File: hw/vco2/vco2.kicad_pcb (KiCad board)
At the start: 4 copper layers, 30 x 128.5 mm, 85 parts, among them J1 Conn_02x08_Odd_Even, Q1 DNP, SW1 SW_SPDT, U1 SSI2131, U2 TL431BCDBZR, U4 TL072HxD, U5 TL072HxD

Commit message: Dual VCO board
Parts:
- removed G***: LOGO, elemental:elemental-4mm
- removed H2, H3, H4: MountingHole, MountingHole:MountingHole_3.5mm
- removed REF**: OSHW-Logo2_7.3x6mm_SilkScreen, Symbol:OSHW-Logo2_7.3x6mm_SilkScreen
- removed RV_CV2: 100k, Pot:RV9012NO
- removed SW1: SW_SPDT, Switch:SPDT big pads
- added C16: 100n, Capacitor_SMD:C_0805_2012Metric_Pad1.18x1.45mm_HandSolder, F.Cu at (56.5, 89.5)
- added C19: 100n, Capacitor_SMD:C_0603_1608Metric_Pad1.08x0.95mm_HandSolder, F.Cu at (153.0, 97.1)
- added C20: 100n, Capacitor_SMD:C_0603_1608Metric_Pad1.08x0.95mm_HandSolder, F.Cu at (153.0, 99.6)
- added C21: 100n, Capacitor_SMD:C_0805_2012Metric_Pad1.18x1.45mm_HandSolder, F.Cu at (179.1, 108.3)
- added C22: 100n, Capacitor_SMD:C_0603_1608Metric_Pad1.08x0.95mm_HandSolder, F.Cu at (153.0, 102.1)
- added C23: 100n, Capacitor_SMD:C_0603_1608Metric_Pad1.08x0.95mm_HandSolder, F.Cu at (153.0, 104.6)
- added C24: 100n X7R, Capacitor_SMD:C_0603_1608Metric_Pad1.08x0.95mm_HandSolder, F.Cu at (195.7, 81.6)
- added C25: 3.9n C0G, Capacitor_SMD:C_0603_1608Metric_Pad1.08x0.95mm_HandSolder, F.Cu at (195.7, 84.1)
- added C26: 10n, Capacitor_SMD:C_0603_1608Metric_Pad1.08x0.95mm_HandSolder, F.Cu at (195.7, 86.7)
- added C27: 100n X7R, Capacitor_SMD:C_0603_1608Metric_Pad1.08x0.95mm_HandSolder, F.Cu at (195.7, 89.2)
- added D3: LED wave out, LED_THT:LED_D3.0mm, F.Cu at (178.4, 98.6)
- added D4: LED wave out, LED_THT:LED_D3.0mm, F.Cu at (178.4, 104.0)
- added JP1: jumper, Jumper:SolderJumper-2_P1.3mm_Bridged2Bar_Pad1.0x1.5mm, F.Cu at (41.4, 85.3)
- added J_PULSE2: TS, Connector_Audio:Jack_3.5mm_QingPu_WQP-PJ398SM_Vertical_CircularHoles, F.Cu at (126.0, 138.2)
- added J_PWM2: TS, Connector_Audio:Jack_3.5mm_QingPu_WQP-PJ398SM_Vertical_CircularHoles, F.Cu at (132.0, 119.2)
- added J_SAW2: TS, Connector_Audio:Jack_3.5mm_QingPu_WQP-PJ398SM_Vertical_CircularHoles, F.Cu at (117.0, 136.2)
- added J_TRI2: TS, Connector_Audio:Jack_3.5mm_QingPu_WQP-PJ398SM_Vertical_CircularHoles, F.Cu at (135.0, 136.2)
- added R36: 32k, Resistor_SMD:R_0603_1608Metric_Pad0.98x0.95mm_HandSolder, F.Cu at (51.9, 93.9)
- added R37: 39k, Resistor_SMD:R_0603_1608Metric_Pad0.98x0.95mm_HandSolder, F.Cu at (51.9, 96.4)
- added R38: 49k9, Resistor_SMD:R_0603_1608Metric_Pad0.98x0.95mm_HandSolder, F.Cu at (51.9, 98.9)
- added R39: 10k, Resistor_SMD:R_0603_1608Metric_Pad0.98x0.95mm_HandSolder, F.Cu at (153.0, 107.1)
- added R40: 20k, Resistor_SMD:R_0603_1608Metric_Pad0.98x0.95mm_HandSolder, F.Cu at (153.0, 109.6)
- added R41: 1k, Resistor_SMD:R_0603_1608Metric_Pad0.98x0.95mm_HandSolder, F.Cu at (153.0, 112.1)
- added R42: 49k9, Resistor_SMD:R_0603_1608Metric_Pad0.98x0.95mm_HandSolder, F.Cu at (157.4, 97.1)
- added R43: 49k9, Resistor_SMD:R_0603_1608Metric_Pad0.98x0.95mm_HandSolder, F.Cu at (157.4, 99.6)
- added R44: 10k, Resistor_SMD:R_0603_1608Metric_Pad0.98x0.95mm_HandSolder, F.Cu at (157.4, 102.1)
- added R45: 250k, Resistor_SMD:R_0603_1608Metric_Pad0.98x0.95mm_HandSolder, F.Cu at (157.4, 104.6)
- added R46: 49k9, Resistor_SMD:R_0603_1608Metric_Pad0.98x0.95mm_HandSolder, F.Cu at (157.4, 107.1)
- added R49: 49k9, Resistor_SMD:R_0603_1608Metric_Pad0.98x0.95mm_HandSolder, F.Cu at (157.4, 109.6)
- added R50: 49k9, Resistor_SMD:R_0603_1608Metric_Pad0.98x0.95mm_HandSolder, F.Cu at (157.4, 112.1)
- added R51: 32k, Resistor_SMD:R_0603_1608Metric_Pad0.98x0.95mm_HandSolder, F.Cu at (161.7, 97.1)
- added R52: 10k, Resistor_SMD:R_0603_1608Metric_Pad0.98x0.95mm_HandSolder, F.Cu at (161.7, 99.6)
- added R53: 10k, Resistor_SMD:R_0603_1608Metric_Pad0.98x0.95mm_HandSolder, F.Cu at (161.7, 102.1)
- added R54: 10k, Resistor_SMD:R_0603_1608Metric_Pad0.98x0.95mm_HandSolder, F.Cu at (161.7, 104.6)
- added R55: 10k, Resistor_SMD:R_0603_1608Metric_Pad0.98x0.95mm_HandSolder, F.Cu at (161.7, 107.1)
- added R56: 39k, Resistor_SMD:R_0603_1608Metric_Pad0.98x0.95mm_HandSolder, F.Cu at (161.7, 109.6)
- added R57: 39k, Resistor_SMD:R_0603_1608Metric_Pad0.98x0.95mm_HandSolder, F.Cu at (161.7, 112.1)
- added R58: 39k, Resistor_SMD:R_0603_1608Metric_Pad0.98x0.95mm_HandSolder, F.Cu at (166.1, 97.1)
- added R59: 39k, Resistor_SMD:R_0603_1608Metric_Pad0.98x0.95mm_HandSolder, F.Cu at (166.1, 99.6)
- added R60: 1k, Resistor_SMD:R_0603_1608Metric_Pad0.98x0.95mm_HandSolder, F.Cu at (166.1, 102.1)
- added R61: 1k, Resistor_SMD:R_0603_1608Metric_Pad0.98x0.95mm_HandSolder, F.Cu at (166.1, 104.6)
- added R62: 1k, Resistor_SMD:R_0603_1608Metric_Pad0.98x0.95mm_HandSolder, F.Cu at (166.1, 107.1)
- added R63: 4k3, Resistor_SMD:R_0603_1608Metric_Pad0.98x0.95mm_HandSolder, F.Cu at (195.7, 91.7)
- added R64: 267k, Resistor_SMD:R_0603_1608Metric_Pad0.98x0.95mm_HandSolder, F.Cu at (195.7, 94.2)
- added R65: 499k, Resistor_SMD:R_0603_1608Metric_Pad0.98x0.95mm_HandSolder, F.Cu at (195.7, 96.7)
- added R66: 20k, Resistor_SMD:R_0603_1608Metric_Pad0.98x0.95mm_HandSolder, F.Cu at (195.7, 99.2)
- added R67: 270, Resistor_SMD:R_0603_1608Metric_Pad0.98x0.95mm_HandSolder, F.Cu at (195.7, 101.7)
- added RV_CALIB2: 10k 3266Y-103, Potentiometer_THT:Potentiometer_Bourns_3266Y_Vertical, F.Cu at (204.5, 94.9)
- added RV_PWM2: 20k, Pot:RV9012NO, F.Cu at (127.8, 65.0)
- added RV_RANGE2: 20k, Pot:RV9012NO, F.Cu at (121.4, 46.6)
- added RV_TUNE2: 20k, Pot:RV9012NO, F.Cu at (134.7, 46.6)
- added TP10: TestPoint_Alt, Holes:TP_0.9mm, F.Cu at (207.7, 96.4)
- added TP9: TestPoint_Alt, Holes:TP_0.9mm, F.Cu at (207.7, 93.4)
- added U3: TL072HxD, Package_SO:SOIC-8_3.9x4.9mm_P1.27mm, F.Cu at (43.5, 71.4)
- added U6: TL431BCDBV, Package_TO_SOT_SMD:SOT-23-5, F.Cu at (35.2, 83.5)
- added U7: TL072HxD, Package_SO:SOIC-8_3.9x4.9mm_P1.27mm, F.Cu at (172.5, 99.2)
- added U8: TL072HxD, Package_SO:SOIC-8_3.9x4.9mm_P1.27mm, F.Cu at (172.5, 105.8)
- added U9: SSI2131, Package_SO:STC_SOP-16_3.9x9.9mm_P1.27mm, F.Cu at (202.1, 86.3)
- C1, C13, C2, C3, C4, C5, C6, C8, J1, Q1, R10, R11, R12, R13, R20, R23, R24, R25, R32, R33, R34, R35, RV_CALIB1, U1: moved to F.Cu
- C7: value 2.2u -> 100n; footprint Capacitor_SMD:C_0805_2012Metric_Pad1.18x1.45mm_HandSolder -> Capacitor_SMD:C_0603_1608Metric_Pad1.08x0.95mm_HandSolder; moved to F.Cu
- D1: value LED sync -> LED wave out
- H1: footprint MountingHole:MountingHole_3.5mm -> MountingHole:MountingHole_3.2mm_M3_Pad
- J_CV1, J_CV2, J_FM1, J_PULSE1, J_PWM1, J_SAW1, J_SYNC1, J_TRI1: value AudioJack2_SwitchT -> TS
- R15: value 49k9 -> 10k; moved to F.Cu
- R16: value 1M -> 250k
- R17: value 49k9 -> 10k
- R18, R19: value 100k -> 49k9
- R27, R8: value 1k -> 39k; moved to F.Cu
- R28: value 0 -> 49k9; moved to F.Cu
- R29: value 0 -> 20k; moved to F.Cu
- R30: value 0 -> 1k; moved to F.Cu
- R31: value 0 -> 10k
- RV_PWM1, RV_RANGE1, RV_TUNE1: value 100k -> 20k
- U2: value TL431BCDBZR -> TL431BCDBZ; moved to F.Cu
- moved J1 109.7 mm to (25.9, 64.1), turned to 0 degrees
- moved TP7 88.5 mm to (178.2, 111.2)
- moved C13 84.7 mm to (34.8, 64.3), turned to 0 degrees
- moved R8 84.0 mm to (34.8, 66.8), turned to 0 degrees
- moved C1 81.8 mm to (34.8, 59.2), turned to 0 degrees
- moved J_CV1 80.2 mm to (90.0, 132.0)
- moved R25 79.7 mm to (39.2, 64.3), turned to 0 degrees
- moved R32 79.2 mm to (43.5, 59.2), turned to 0 degrees
- moved R33 78.7 mm to (43.5, 61.7), turned to 0 degrees
- moved C7 78.2 mm to (34.8, 61.7)
- moved R34 74.3 mm to (43.5, 64.3), turned to 0 degrees
- moved R35 72.5 mm to (43.5, 66.8), turned to 0 degrees
- moved J_CV2 71.2 mm to (121.0, 118.9), turned to 0 degrees
- moved TP3 66.5 mm to (45.7, 76.1)
- moved C2 65.8 mm to (34.8, 71.3), turned to 0 degrees
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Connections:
- net /BW_COMP renamed /Oscillator 1/BW_COMP
- net /LIN_FREQ renamed /LIN_FREQ1
- net /PULSE_OUT renamed /PULSE1
- net /SAW_OUT renamed /SAW1
- C1 pad 1: +2V5 -> +12V
- C10 pad 2: /HARD_SYNC -> /HARD_SYNC1
- C6 pad 1: /TCAP -> /Oscillator 1/TCAP
- C7 pad 1: /TCAP -> GND
- C7 pad 2: Net-(SW1-A) -> -12V
- D1 pad 2: /HARD_SYNC -> GND
- D2 pad 1: Net-(D2-K) -> GND
- D2 pad 2: Net-(D2-A) -> Net-(D1-K)
- J1 pad 14: unconnected-(J1-Pin_14-Pad14) -> Net-(J1-Pin_14)
- J_CV1 pad TN: GND -> BACKPLANE_CV
- J_CV2 pad TN: unconnected-(J_CV2-PadTN) -> Net-(J_CV1-PadT)
- J_PULSE1 pad T: Net-(J_PULSE1-PadT) -> Net-(C16-Pad2)
- Q1 pad 2: /HARD_SYNC -> ANTI_HANGUP
- R11 pad 1: /HF_TRACK -> /Oscillator 1/HF_TRACK
- R11 pad 2: /EXPO_FREQ -> /EXPO_FREQ1
- R12 pad 1: /HF_TRACK -> /Oscillator 1/HF_TRACK
- R14 pad 2: /EXPO_FREQ -> /EXPO_FREQ1
- R15 pad 1: Net-(R15-Pad1) -> Net-(U5B--)
- R15 pad 2: /EXPO_FREQ -> /TRI1
- R16 pad 2: /EXPO_FREQ -> /EXPO_FREQ1
- R17 pad 2: /EXPO_FREQ -> /EXPO_FREQ1
- R18 pad 2: /PWM_CTRL -> Net-(R18-Pad2)
- R19 pad 2: /PWM_CTRL -> Net-(R18-Pad2)
- R22 pad 1: /HARD_SYNC -> /HARD_SYNC1
- R25 pad 1: +2V5 -> Net-(U2-K)
- R26 pad 1: Net-(D2-K) -> Net-(R26-Pad1)
- R26 pad 2: GND -> Net-(D1-K)
- R27 pad 1: Net-(D1-K) -> Net-(U3B--)
- R27 pad 2: GND -> -2V5
- R28 pad 1: GND -> Net-(R18-Pad2)
- R28 pad 2: Net-(R28-Pad2) -> /PWM_CTRL1
- R29 pad 2: +12V -> +2V5
- R31 pad 2: +12V -> +2V5
- R32 pad 2: /OPREF -> OPREF
- R33 pad 1: /OPREF -> OPREF
- R4 pad 1: Net-(R4-Pad1) -> Net-(C16-Pad1)
- R7 pad 2: /TRI_OUT -> /TRI1
- R8 pad 1: Net-(J_PULSE1-PadT) -> +2V5
- R8 pad 2: Net-(R4-Pad1) -> Net-(U3B--)
- RV_PWM1 pad 1: +2V5 -> Net-(R29-Pad1)
- RV_PWM1 pad 2: /PWM_CTRL -> Net-(R38-Pad1)
- RV_PWM1 pad 3: GND -> Net-(R30-Pad2)
- RV_RANGE1 pad 1: Net-(R31-Pad1) -> GND
- RV_RANGE1 pad 3: Net-(R30-Pad2) -> Net-(R31-Pad1)
- RV_TUNE1 pad 1: Net-(R29-Pad1) -> GND
- RV_TUNE1 pad 3: Net-(R28-Pad2) -> +2V5
- TP1 pad 1: /TRI_OUT -> /TRI1
- TP2 pad 1: /EXPO_FREQ -> /EXPO_FREQ1
- TP5 pad 1: /HF_TRACK -> -2V5
- TP6 pad 1: /TCAP -> /Oscillator 1/TCAP
- TP7 pad 1: GND -> /EXPO_FREQ2
- U1 pad 10: /HARD_SYNC -> /HARD_SYNC1
- U1 pad 3: /PWM_CTRL -> /PWM_CTRL1
- U1 pad 4: /TRI_OUT -> /TRI1
- U1 pad 5: /HF_TRACK -> /Oscillator 1/HF_TRACK
- U1 pad 6: /EXPO_FREQ -> /EXPO_FREQ1
- U1 pad 8: /TCAP -> /Oscillator 1/TCAP
- U2 pad 1: +2V5 -> Net-(U2-K)
- U2 pad 2: +2V5 -> Net-(U2-K)
- U4 pad 3: /OPREF -> OPREF
- U4 pad 5: /OPREF -> OPREF
- U4 pad 7: Net-(R4-Pad1) -> Net-(C16-Pad1)
- U5 pad 3: /OPREF -> OPREF
- U5 pad 5: Net-(U5A--) -> OPREF
- U5 pad 6: /OPREF -> Net-(U5B--)
- U5 pad 7: Net-(D2-A) -> Net-(R26-Pad1)
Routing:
- net +12V: track 144.5 -> 0.00 mm, vias 2 -> 0
- net -12V: track 129.5 -> 0.00 mm, vias 4 -> 0
- net +5V: track 103.5 -> 0.00 mm, vias 5 -> 0
- net +2V5: track 90.5 -> 0.00 mm, vias 2 -> 0
- net /EXPO_FREQ: track 64.9 -> 0.00 mm
- net GND: track 58.1 -> 0.00 mm, vias 15 -> 0
- net /HARD_SYNC: track 37.9 -> 0.00 mm, vias 2 -> 0
- net /OPREF: track 34.7 -> 0.00 mm
- net /LIN_FREQ1: track 33.2 -> 0.00 mm
- net /PWM_CTRL: track 32.2 -> 0.00 mm
- net /SAW1: track 30.0 -> 0.00 mm
- net /TRI_OUT: track 28.9 -> 0.00 mm
- net /PULSE1: track 28.0 -> 0.00 mm
- net Net-(J_CV2-PadT): track 27.6 -> 0.00 mm
- net Net-(J_CV1-PadT): track 25.4 -> 0.00 mm
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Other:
- board size 30 x 128.5 mm -> 60 x 110 mm
- board text added: "12 HP Eurorack"
- board text added: "VCO2 rev1 Elemental Instruments Jonas Norling 2026"
- board text removed: "6 HP Eurorack"
- board text removed: "CV1"
- board text removed: "CV2"
- board text removed: "CV2 DEPTH"
- board text removed: "DJUP"
- board text removed: "FM"
- board text removed: "OCTAVE"
- board text removed: "OKTAV"
- board text removed: "OMFÅNG"
- board text removed: "PULS"
- board text removed: "PULSE"
- board text removed: "PWM"
- board text removed: "SAKTA"
- board text removed: "SAW"
- board text removed: "SNABB"
- board text removed: "STÄM"
- board text removed: "SYNC"
- board text removed: "SYNK"
- board text removed: "SÅGTAND"
- board text removed: "TRIANGEL"
- board text removed: "TRIANGLE"
- board text removed: "TUNE"
- board text removed: "Tongenerator SSI2131"
- board text removed: "VCO rev1 Elemental Instruments Jonas Norling 2026"
- board text removed: "prototyp 1"

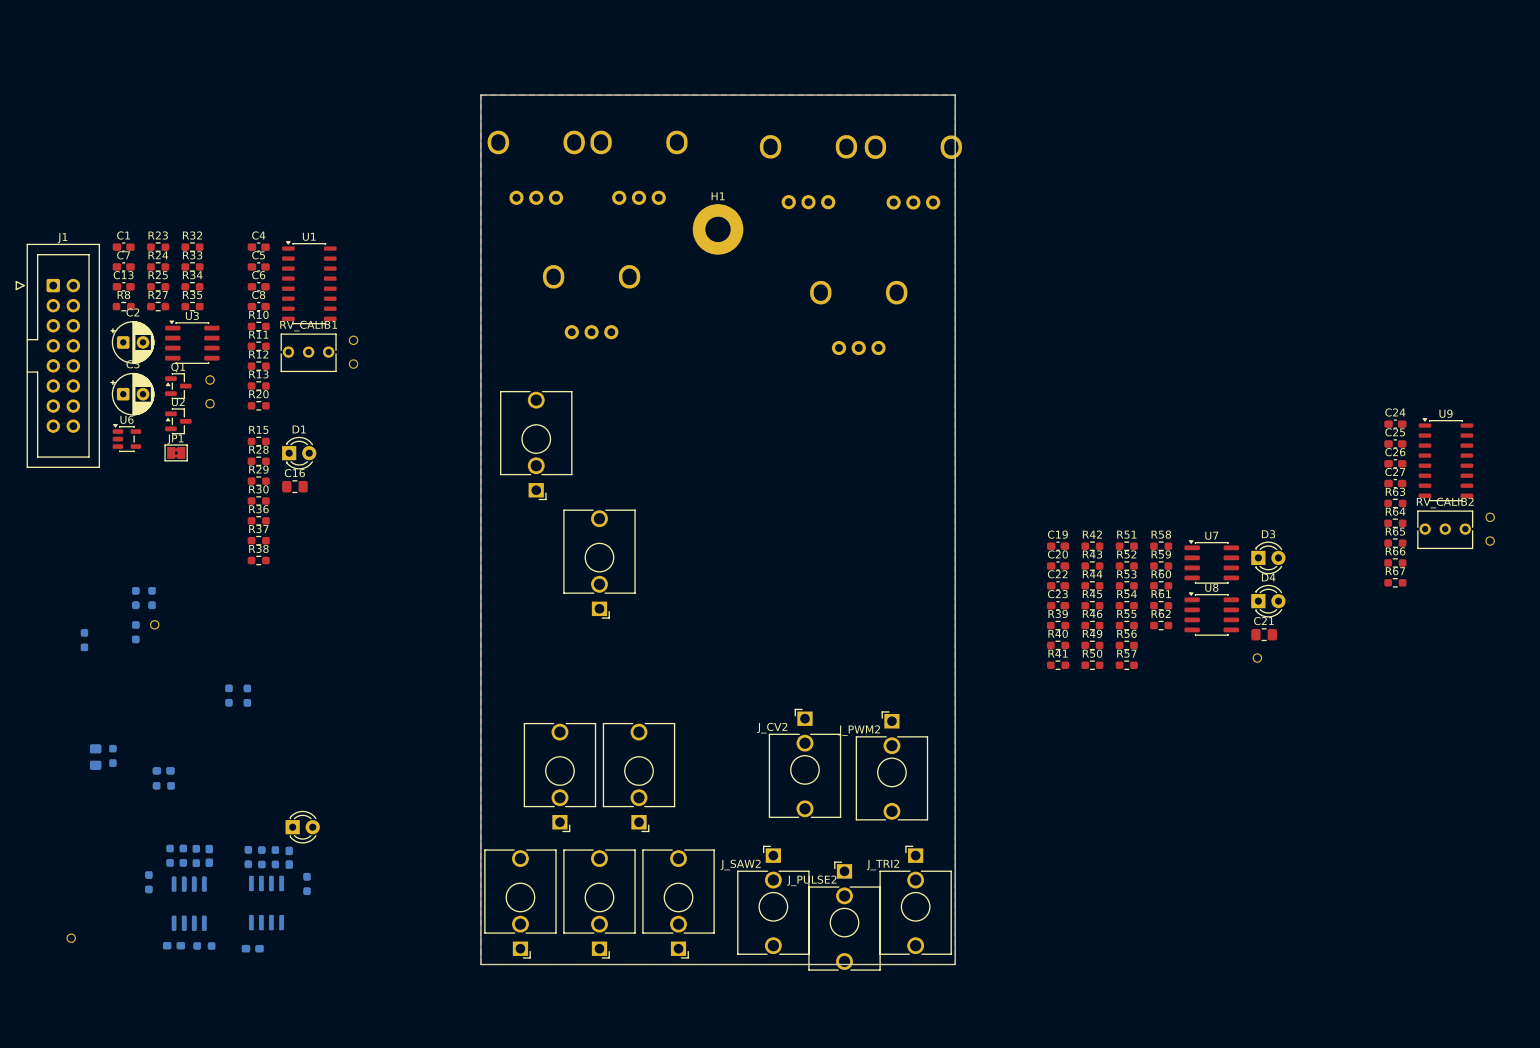
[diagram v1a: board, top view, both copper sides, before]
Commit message: Layout VCO2 board
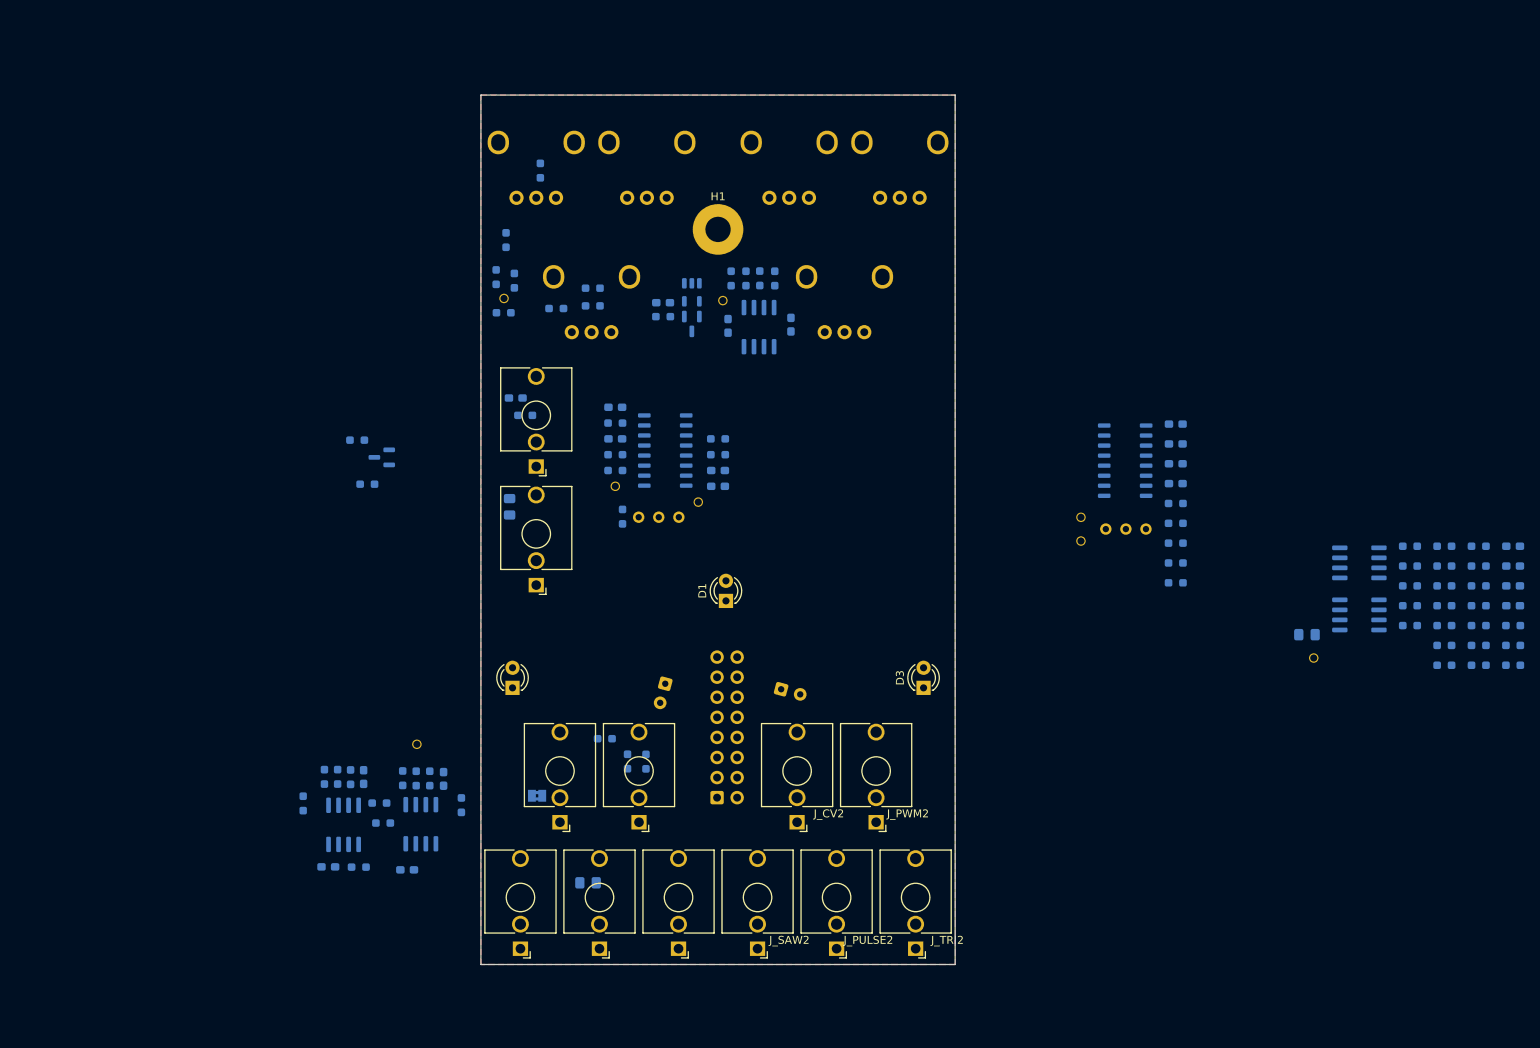
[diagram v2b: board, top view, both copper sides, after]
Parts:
- removed D4: LED wave out, LED_THT:LED_D3.0mm
- removed R27, R8: 39k, Resistor_SMD:R_0603_1608Metric_Pad0.98x0.95mm_HandSolder
- removed TP5: TestPoint_Alt, Holes:TP_0.9mm
- C1, C13, C16, C19, C2, C20, C21, C22, C23, C24, C25, C26, C27, C3, C4, C5, C6, C7, C8, JP1, Q1, R10, R11, R12, R13, R15, R20, R23, R24, R25, R28, R29, R30, R32, R33, R34, R35, R36, R37, R38, R39, R40, R41, R42, R43, R44, R45, R46, R49, R50, R51, R52, R53, R54, R55, R56, R57, R58, R59, R60, R61, R62, R63, R64, R65, R66, R67, RV_CALIB1, RV_CALIB2, TP1, TP10, TP3, TP6, TP7, TP9, U1, U2, U3, U6, U7, U8, U9: moved to B.Cu
- D1: value LED wave out -> LED diff
- J1: footprint Connector_IDC:IDC-Header_2x08_P2.54mm_Vertical -> Eurorack:IDC-Header_2x08_P2.54mm_Vertical; moved to B.Cu
- moved J1 106.1 mm to (109.9, 128.9)
- moved C2 94.1 mm to (118.0, 115.2), turned to -15 degrees
- moved TP4 89.5 mm to (97.0, 89.5)
- moved C7 84.7 mm to (119.2, 69.0), turned to 90 degrees
- moved R31 82.8 mm to (87.5, 49.6)
- moved C3 77.7 mm to (103.3, 114.5), turned to -105 degrees
- moved C1 77.1 mm to (111.3, 69.2), turned to 90 degrees
- moved U6 73.8 mm to (106.7, 65.0), turned to -90 degrees
- moved R35 73.8 mm to (117.2, 63.2), turned to -90 degrees
- moved R21 73.1 mm to (97.0, 87.5), turned to 0 degrees
- moved R34 71.8 mm to (115.3, 63.2), turned to -90 degrees
- moved U3 71.7 mm to (115.2, 69.4), turned to -90 degrees
- moved R33 70.0 mm to (113.5, 63.2), turned to -90 degrees
- moved C13 68.3 mm to (103.0, 66.3), turned to 180 degrees
- moved R32 68.3 mm to (111.7, 63.2), turned to -90 degrees
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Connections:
- D1 pad 2: GND -> Net-(D1-A)
- D2 pad 2: Net-(D1-K) -> Net-(D1-A)
- D3 pad 2: Net-(D3-A) -> Net-(D1-K)
- R26 pad 2: Net-(D1-K) -> Net-(D1-A)
- R62 pad 2: Net-(D3-A) -> Net-(D1-K)
- U3 pad 6: Net-(U3B--) -> GND
- U3 pad 7: -2V5 -> unconnected-(U3-Pad7)
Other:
- board text removed: "-12V"

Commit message: Place components
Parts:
- moved R39 108.5 mm to (119.0, 49.0)
- moved R40 97.0 mm to (124.0, 66.0), turned to 90 degrees
- moved R41 94.6 mm to (128.0, 66.0), turned to -90 degrees
- moved C19 92.2 mm to (120.0, 114.0), turned to -90 degrees
- moved R60 86.5 mm to (118.0, 136.0), turned to 90 degrees
- moved R42 86.0 mm to (126.0, 66.0), turned to -90 degrees
- moved C20 84.6 mm to (126.0, 102.0), turned to -90 degrees
- moved R56 82.2 mm to (120.0, 102.0), turned to 90 degrees
- moved C22 80.8 mm to (130.0, 108.0), turned to -90 degrees
- moved R46 80.4 mm to (136.0, 68.0)
- moved R45 80.2 mm to (136.0, 66.0), turned to 0 degrees
- moved R52 79.9 mm to (122.0, 102.0), turned to 90 degrees
- moved R57 79.9 mm to (122.0, 114.0), turned to 90 degrees
- moved R44 79.9 mm to (136.0, 64.0), turned to 0 degrees
- moved R43 79.1 mm to (132.0, 127.0), turned to 0 degrees
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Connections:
- C10 pad 2: /HARD_SYNC1 -> ANTI_HANGUP
- R22 pad 1: /HARD_SYNC1 -> ANTI_HANGUP
- U1 pad 10: /HARD_SYNC1 -> ANTI_HANGUP
- U9 pad 10: /Oscillator 2/HARD_SYNC -> ANTI_HANGUP

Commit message: Layout board
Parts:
- added H2: MountingHole, Holes:MountingHole_3.2mm_M3_Pad, F.Cu at (70.0, 66.5)
- added H3: MountingHole, Holes:MountingHole_3.2mm_M3_Pad, F.Cu at (70.0, 74.5)
- H1: footprint MountingHole:MountingHole_3.2mm_M3_Pad -> Holes:MountingHole_3.2mm_M3_Pad
- TP2, TP4: moved to B.Cu
- moved D1 1.00 mm to (110.0, 104.0)
- turned TP2 to 180 degrees
- turned TP4 to 180 degrees
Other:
- board text added: "CV"
- board text added: "FM IN"
- board text added: "PULSE"
- board text added: "PULSE WIDTH"
- board text added: "PWM"
- board text added: "RANGE"
- board text added: "SAW"
- board text added: "SYNC IN"
- board text added: "TRIANGLE"
- board text added: "TUNE"

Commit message: Routing
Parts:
- added G***: LOGO, elemental:elemental-25.4mm, F.Cu at (125.0, 78.5)
- added G***: LOGO, elemental:elemental-4mm-mask, B.Cu at (100.1, 141.0)
- moved H3 67.8 mm to (136.0, 59.0)
- moved H2 15.9 mm to (84.0, 59.0)
- moved TP9 12.8 mm to (135.5, 90.0)
- moved R59 3.00 mm to (135.0, 108.1)
- moved R32 2.35 mm to (114.0, 63.0), turned to 90 degrees
- moved R18 2.00 mm to (97.0, 125.0)
- moved R19 2.00 mm to (97.0, 127.0)
- moved R43 2.00 mm to (132.0, 125.0)
- moved R49 2.00 mm to (132.0, 127.0), turned to 0 degrees
- moved TP2 1.76 mm to (84.5, 72.0)
- moved TP1 1.75 mm to (97.9, 96.2)
- moved R33 1.54 mm to (112.0, 63.0)
- moved R62 1.50 mm to (132.5, 108.0)
- moved R35 0.85 mm to (118.0, 63.0), turned to 90 degrees
- moved R34 0.74 mm to (116.0, 63.0), turned to 90 degrees
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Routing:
- net +2V5: track 0.00 -> 161.5 mm, vias 0 -> 1
- net +5V: track 0.00 -> 95.6 mm, vias 0 -> 4
- net GND: track 0.00 -> 76.0 mm, vias 0 -> 20
- net +12V: track 0.00 -> 65.2 mm, vias 0 -> 1
- net -12V: track 0.00 -> 58.5 mm
- net OPREF: track 0.00 -> 23.9 mm
- net Net-(R16-Pad1): track 0.00 -> 22.1 mm
- net Net-(R44-Pad1): track 0.00 -> 21.3 mm
- net /PWM_CTRL2: track 0.00 -> 15.9 mm
- net Net-(R45-Pad1): track 0.00 -> 15.5 mm
- net /EXPO_FREQ2: track 0.00 -> 14.8 mm
- net Net-(U8B--): track 0.00 -> 14.5 mm
- net Net-(R17-Pad1): track 0.00 -> 13.7 mm
- net Net-(U2-K): track 0.00 -> 13.7 mm
- net /EXPO_FREQ1: track 0.00 -> 12.3 mm
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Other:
- rule pad_to_mask_clearance: 0.05 -> 0

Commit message: Route board
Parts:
- moved G*** 2.40 mm to (100.1, 143.4)
- moved TP6 0.50 mm to (107.5, 86.5)
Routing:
- net -12V: track 58.5 -> 203.6 mm, vias 0 -> 6
- net Net-(J_CV1-PadT): track 0.00 -> 126.3 mm, vias 0 -> 1
- net OPREF: track 23.9 -> 140.0 mm, vias 0 -> 7
- net /PWM_CTRL1: track 0.00 -> 93.3 mm, vias 0 -> 3
- net ANTI_HANGUP: track 2.02 -> 74.9 mm, vias 0 -> 2
- net Net-(J_CV2-PadT): track 0.00 -> 64.4 mm, vias 0 -> 1
- net Net-(J1-Pin_14): track 0.00 -> 62.7 mm
- net /PWM_CTRL2: track 15.9 -> 68.9 mm, vias 0 -> 2
- net Net-(D1-A): track 0.00 -> 49.6 mm, vias 0 -> 2
- net Net-(R58-Pad1): track 3.07 -> 45.2 mm, vias 0 -> 2
- net /SAW1: track 0.00 -> 38.7 mm, vias 0 -> 2
- net /PULSE1: track 0.00 -> 37.0 mm, vias 0 -> 2
- net Net-(R5-Pad1): track 3.07 -> 40.0 mm
- net +2V5: track 161.5 -> 197.4 mm, vias 1 -> 4
- net Net-(R56-Pad1): track 3.07 -> 34.0 mm
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- added copper zone on B.Cu, net GND
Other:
- board text added: "Eurorack dual VCO"
